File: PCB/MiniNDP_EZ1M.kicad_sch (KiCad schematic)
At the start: 16 parts, among them J1 Conn_02x20_Odd_Even, U1 AS6C8008_TSOPII, U2 HC238, U3 4040, U4 FCT841

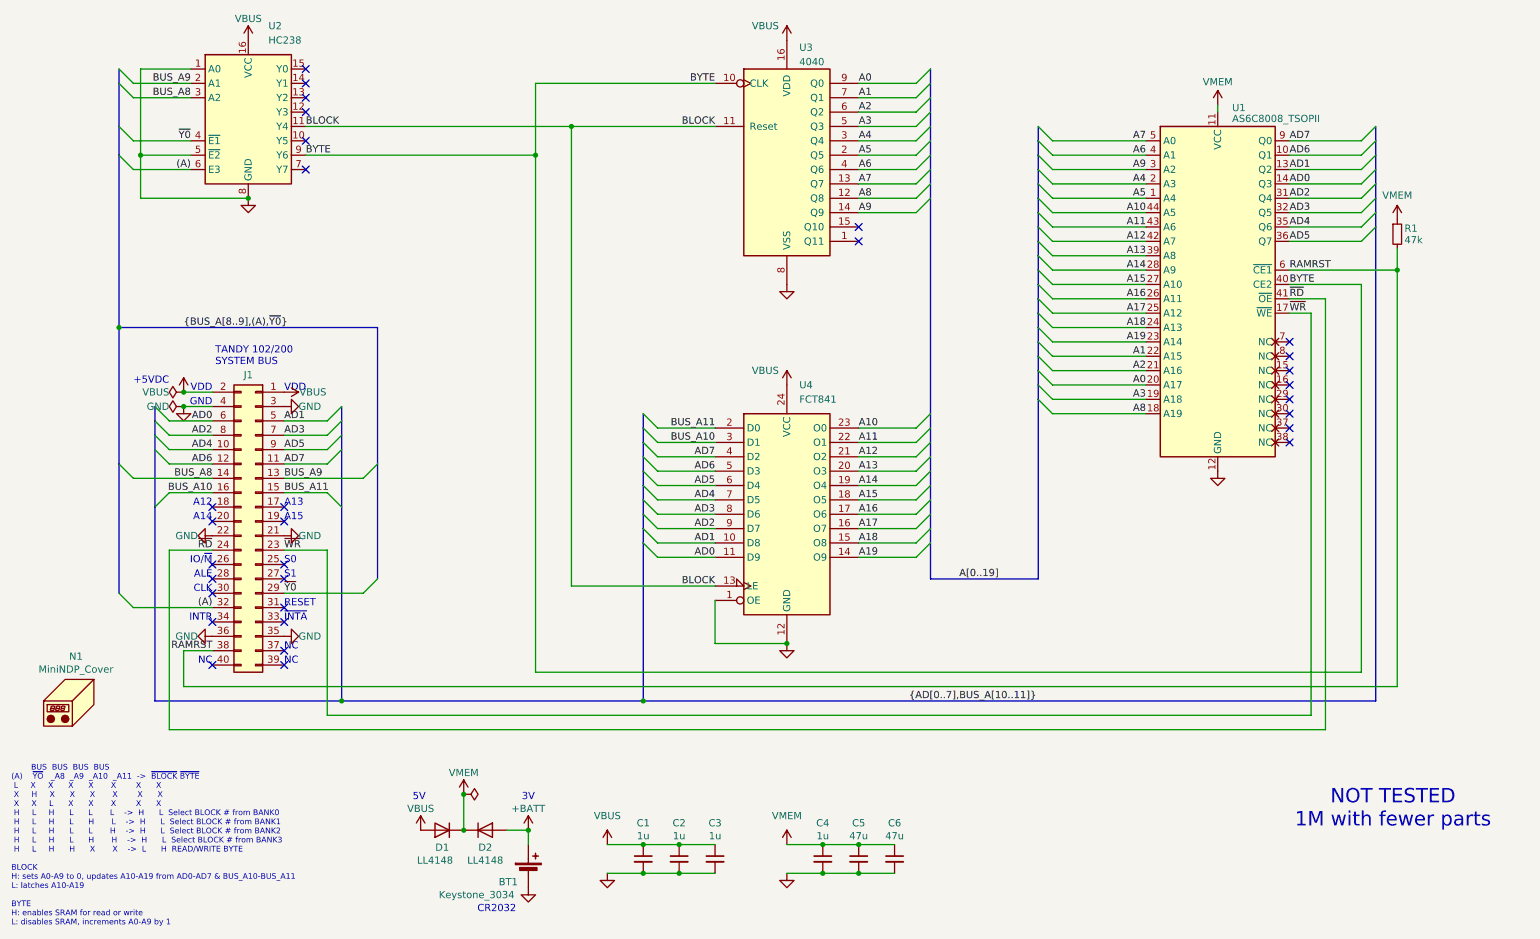
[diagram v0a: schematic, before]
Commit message: add SL1M, rename 1M_C to EZ1M, remove 256_F & 512_F from readme
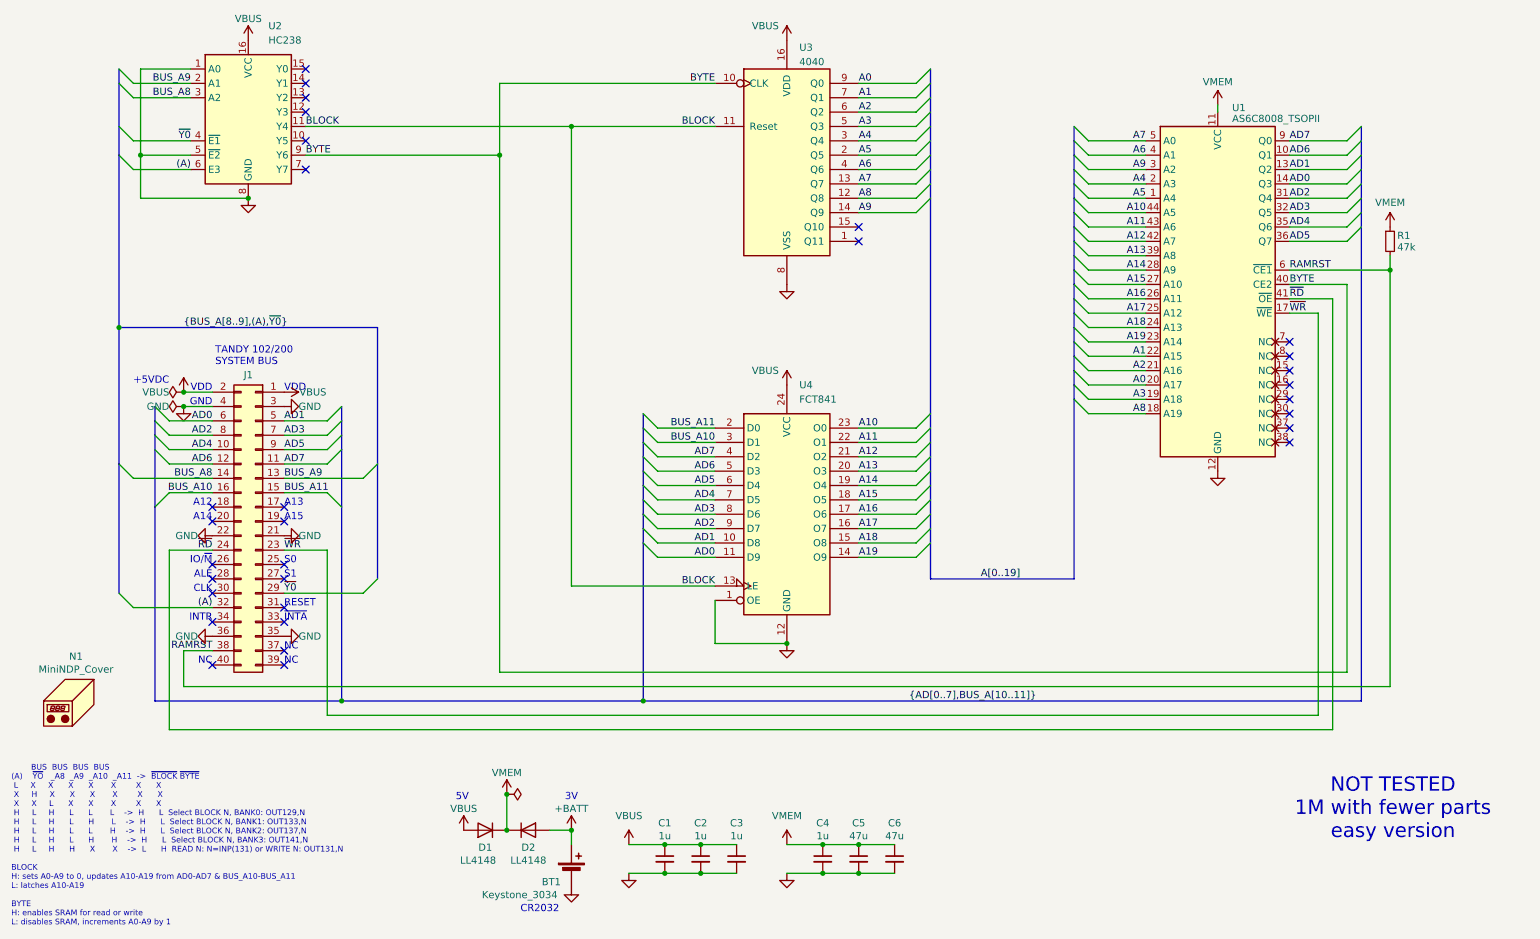
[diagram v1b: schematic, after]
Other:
- note added: "BUS BUS BUS BUS (A) ~{YO} _A8 _A9 _A10 _A11 -> ~{BLOCK} ~{BYTE} L X X X X X X X X H X X X X X X X X L X X X X X H L H L L L -> H L Select BLOCK N, BANK0: OUT129,N H L H L H L -> H L Select BLOCK N, BANK1: OUT133,N H L H L L H -> H L Select BLOCK N, BANK2: OUT137,N H L H L H H -> H L Select BLOCK N, BANK3: OUT141,N H L H H X X -> L H READ N: N=INP(131) or WRITE N: OUT131,N BLOCK H: sets A0-A9 to 0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"
- note added: "NOT TESTED 1M with fewer parts easy version"
- note removed: "BUS BUS BUS BUS (A) ~{YO} _A8 _A9 _A10 _A11 -> ~{BLOCK} ~{BYTE} L X X X X X X X X H X X X X X X X X L X X X X X H L H L L L -> H L Select BLOCK # from BANK0 H L H L H L -> H L Select BLOCK # from BANK1 H L H L L H -> H L Select BLOCK # from BANK2 H L H L H H -> H L Select BLOCK # from BANK3 H L H H X X -> L H READ/WRITE BYTE BLOCK H: sets A0-A9 to 0, updates A10-A19 from AD0-AD7 & BUS_A10-BUS_A11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"
- note removed: "NOT TESTED 1M with fewer parts"
- title: MiniNDP 1M -> MiniNDP EZ1M
- moved on the sheet: BT1, C1, C2, C3, D1, D2, R1

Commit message: EZ1M is tested
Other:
- note added: "1M with fewer parts easy-build version"
- note removed: "NOT TESTED 1M with fewer parts easy version"
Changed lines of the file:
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@@
 		)
 	)
-	(text "NOT TESTED\n1M with fewer parts\neasy version"
+	(text "1M with fewer parts\neasy-build version"
 		(exclude_from_sim no)
 		(at 259.588 173.99 0)
